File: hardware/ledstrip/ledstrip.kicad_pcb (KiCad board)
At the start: 4 copper layers, 118 parts, among them J1 Conn_ARM_JTAG_SWD_10, J2 USB_C_Receptacle_USB2.0_16P, J4 BMS connectors, J5 Ledstrip connector, J6 Header for STUSB4500 I2C, Q1 Q_NMOS, Q10 Q_PMOS, Q11 Q_NMOS, Q2 Q_NMOS, Q3 Q_NMOS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

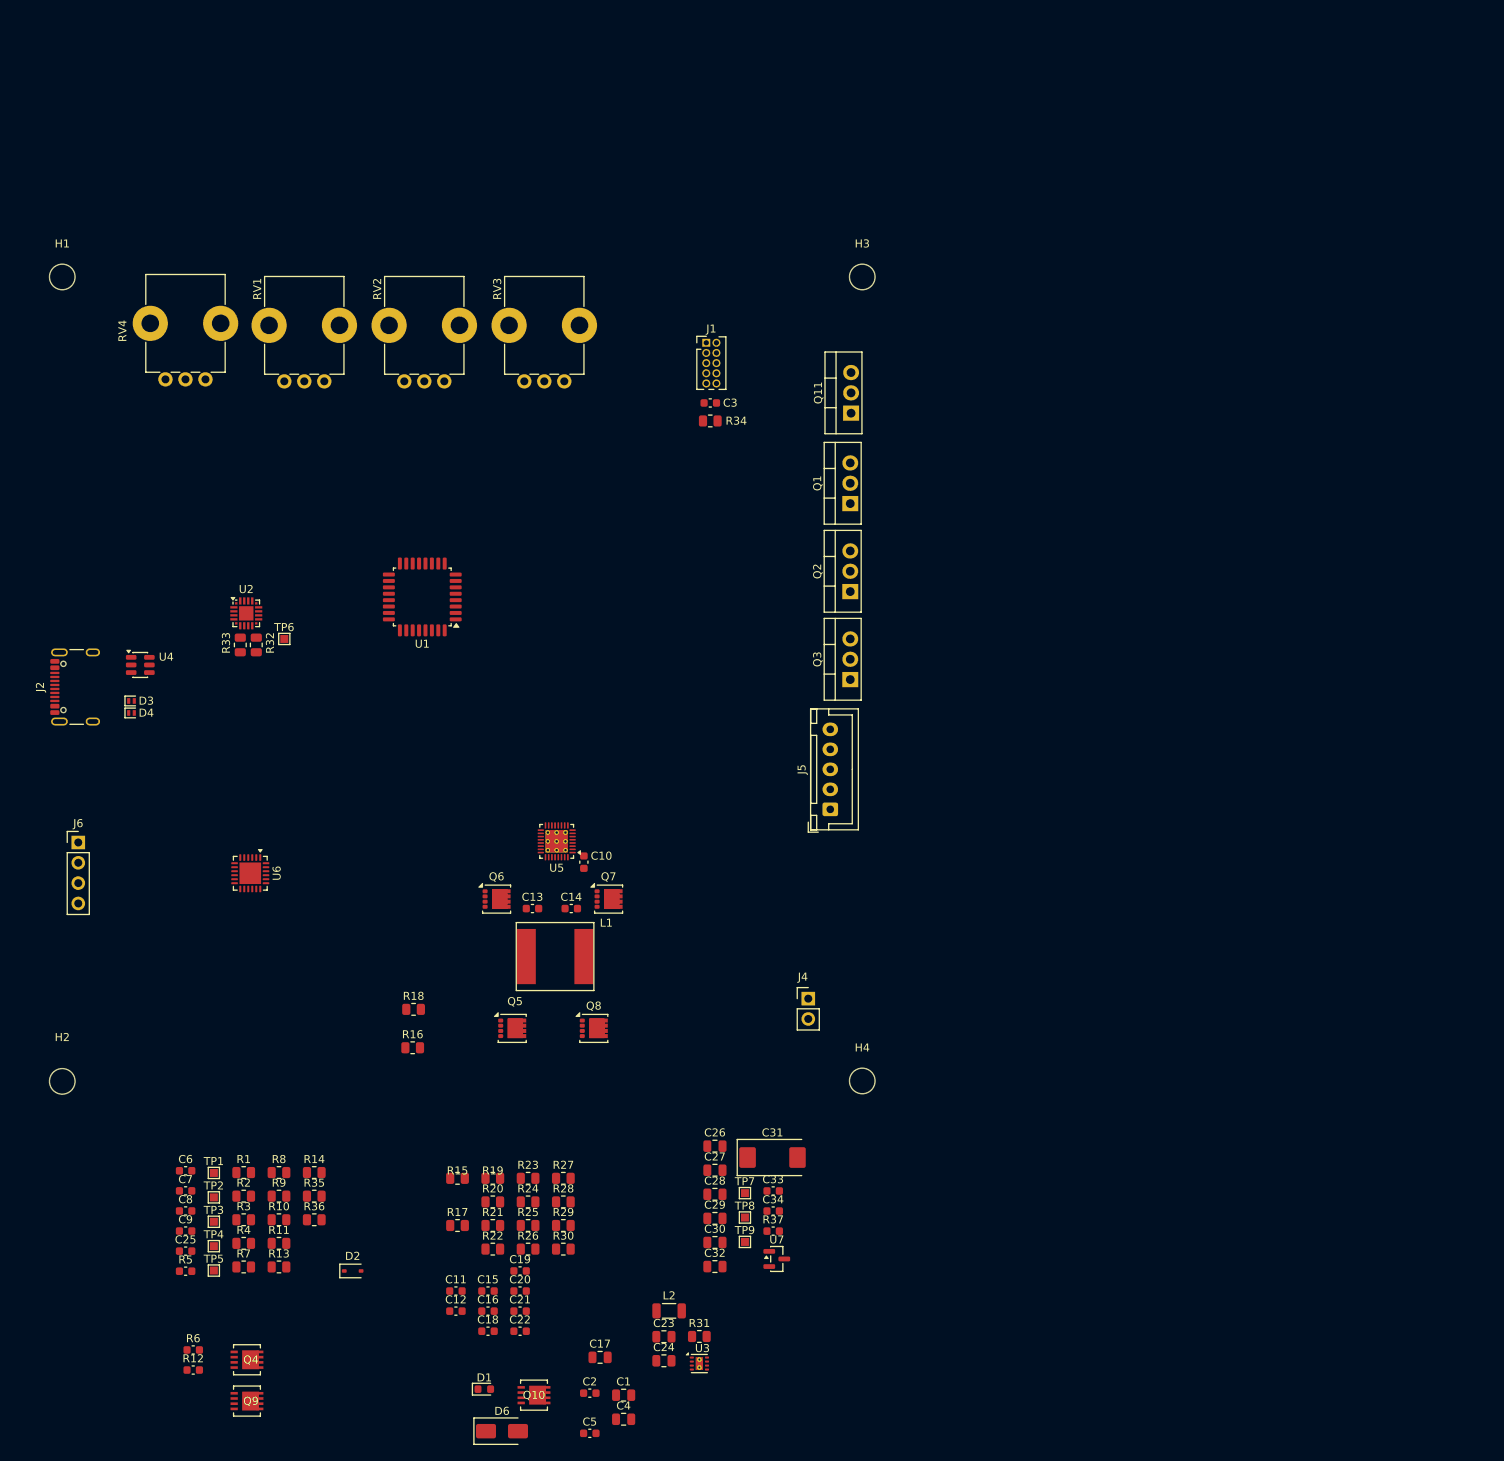
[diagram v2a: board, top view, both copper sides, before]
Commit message: Improve footprint placements.
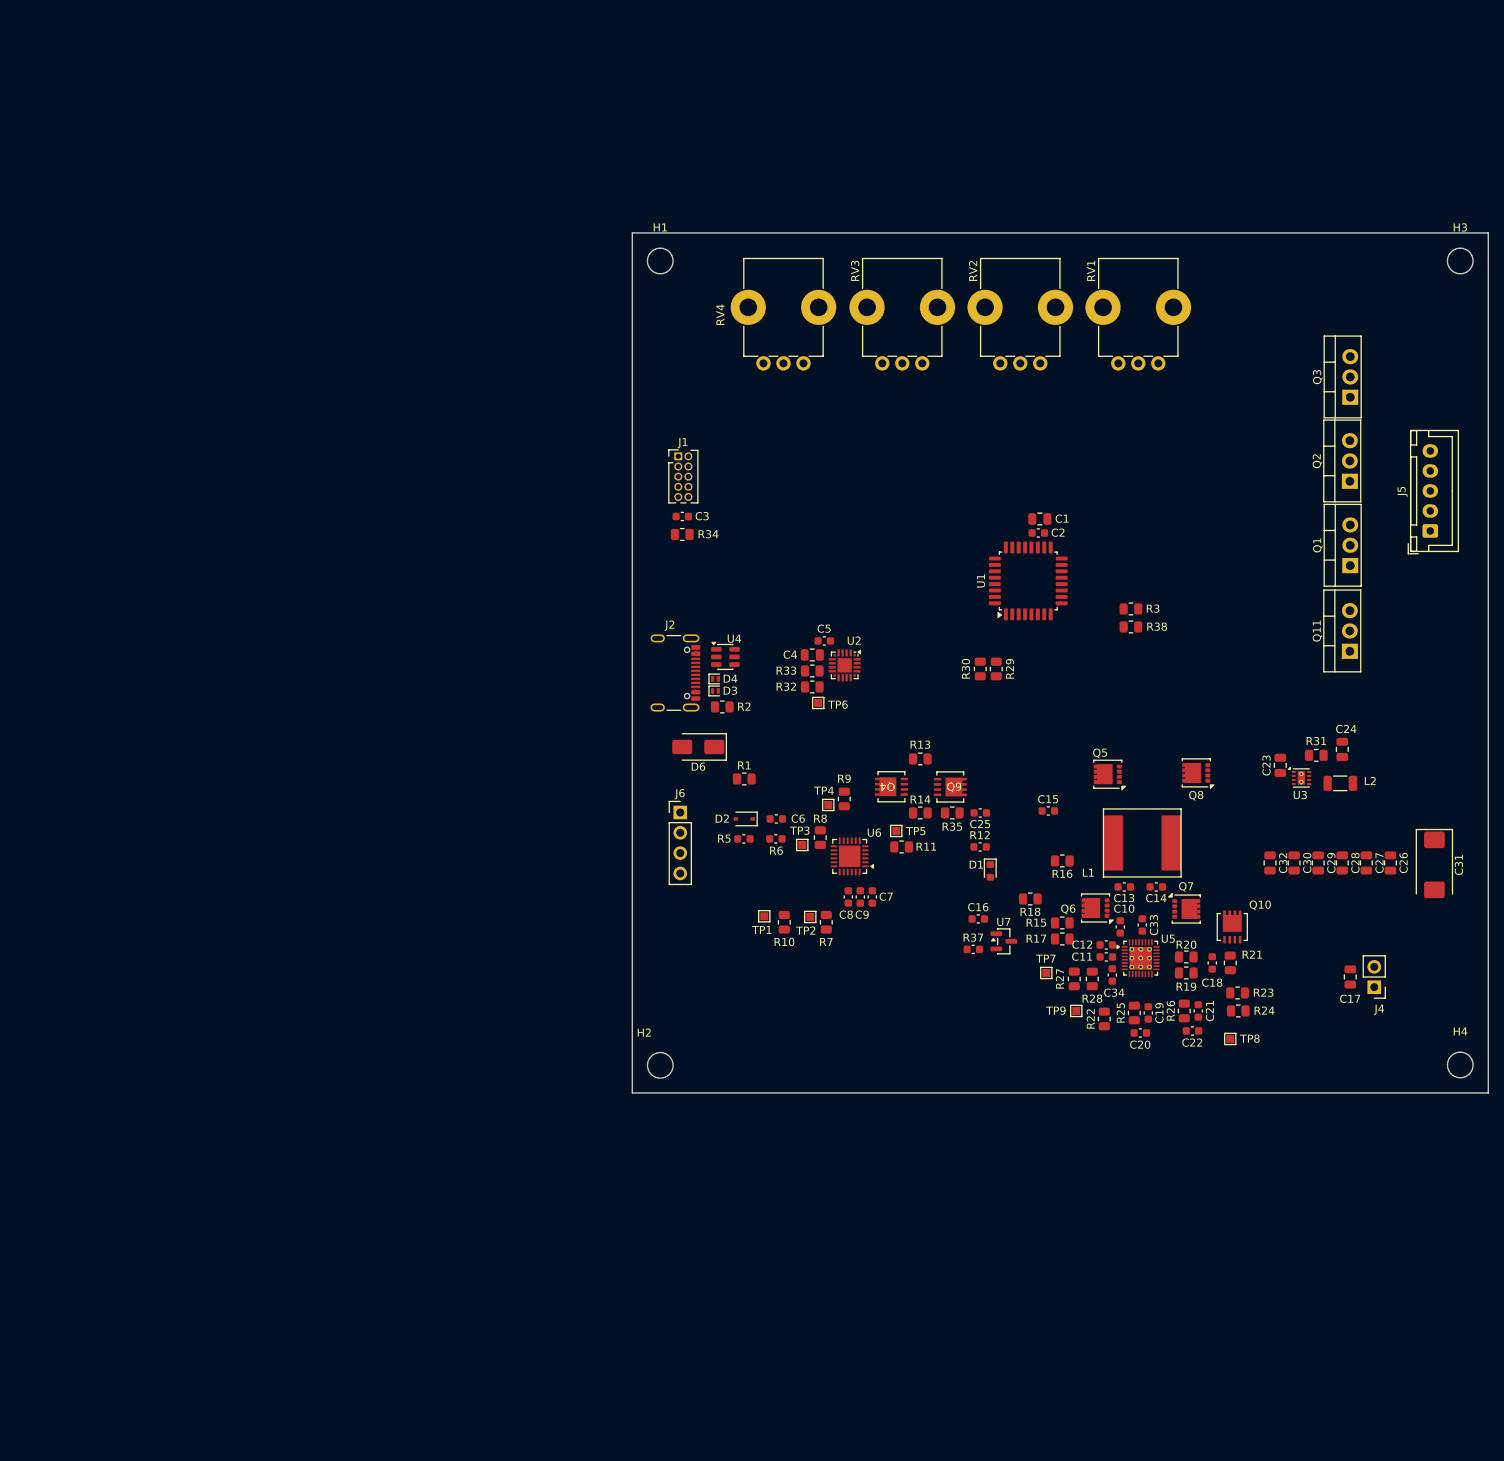
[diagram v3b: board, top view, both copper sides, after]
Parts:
- removed R36: 100K, Resistor_SMD:R_0805_2012Metric
- removed R4: 4,7K, Resistor_SMD:R_0805_2012Metric
- added R38: 10k, Resistor_SMD:R_0805_2012Metric, F.Cu at (158.6, 94.0)
- R3: value 4,7K -> 10k
- moved R3 134.6 mm to (158.6, 91.8)
- moved C2 121.3 mm to (147.0, 82.2)
- moved C1 121.3 mm to (147.2, 80.5)
- moved R12 118.1 mm to (139.7, 121.5)
- moved Q9 116.7 mm to (136.0, 114.0)
- moved C24 114.2 mm to (185.0, 109.3), turned to 90 degrees
- moved C25 113.4 mm to (139.8, 117.2), turned to 180 degrees
- moved Q4 107.8 mm to (128.6, 114.0), turned to 180 degrees
- moved L2 106.7 mm to (184.8, 113.5)
- moved R31 105.9 mm to (181.8, 110.0), turned to 180 degrees
- moved C17 105.1 mm to (186.0, 137.8), turned to -90 degrees
- moved Q10 105.1 mm to (171.2, 131.5), turned to 90 degrees
- moved C23 105.1 mm to (177.2, 111.3), turned to 90 degrees
- moved U3 105.0 mm to (179.9, 112.9)
- moved RV1 104.3 mm to (162.0, 61.0)
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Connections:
- J6 pad 2: /USB PD/STUSB4500_I2C_HEADER_SCL -> /Battery Charger/BQ25703A_SCL
- J6 pad 3: /USB PD/STUSB4500_I2C_HEADER_SDA -> /Battery Charger/BQ25703A_SDA
- R1 pad 2: /USB PD/STUSB4500_VSYS -> +3.3V
- R3 pad 1: /USB PD/STUSB4500_VSYS -> /Battery Charger/BQ25703A_SDA
- R3 pad 2: /USB PD/STUSB4500_I2C_HEADER_SDA -> +3.3V
- U6 pad 24: /USB PD/STUSB4500_VSYS -> +3.3V
- U6 pad 7: /USB PD/STUSB4500_I2C_HEADER_SCL -> /Battery Charger/BQ25703A_SCL
- U6 pad 8: /USB PD/STUSB4500_I2C_HEADER_SDA -> /Battery Charger/BQ25703A_SDA
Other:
- board outline added: 107 x 107.5 mm

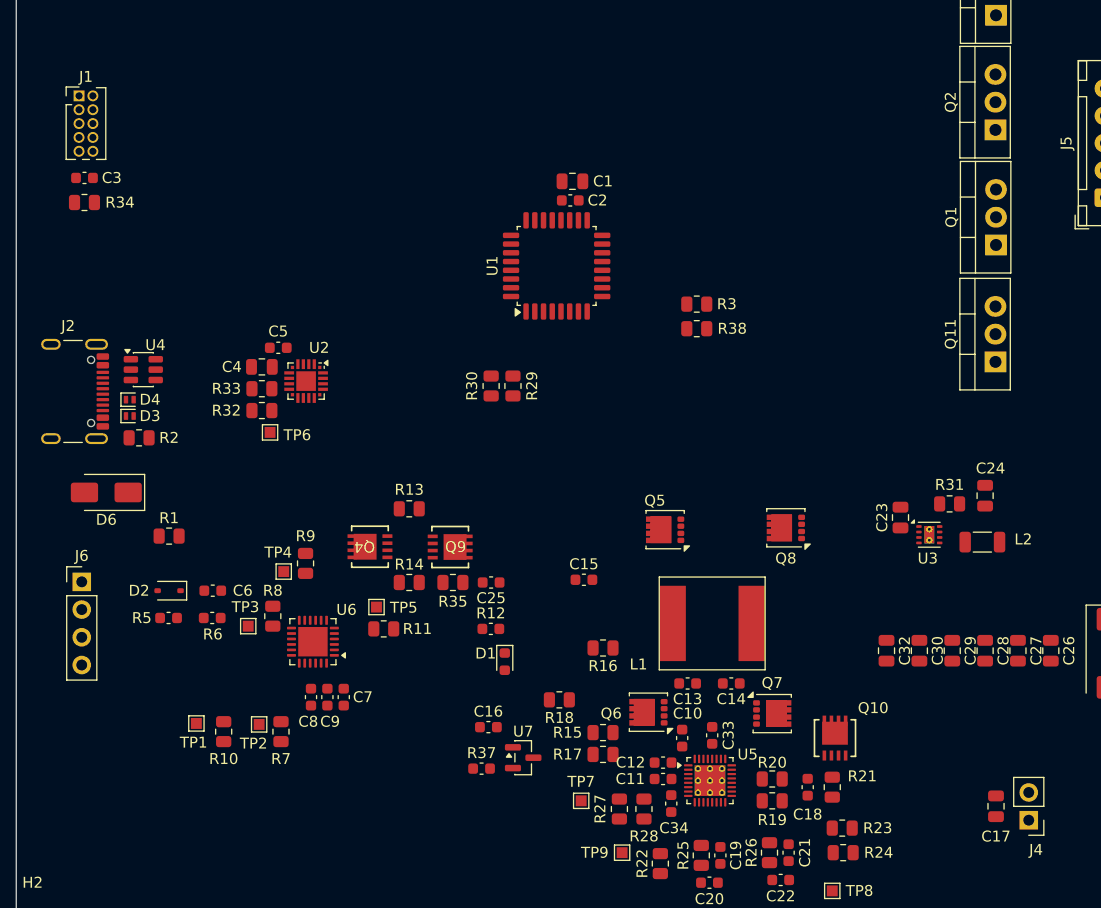
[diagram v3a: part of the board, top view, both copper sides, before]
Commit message: Improve slightly placements.
Add next step in README.md.
Add description of layers usages.
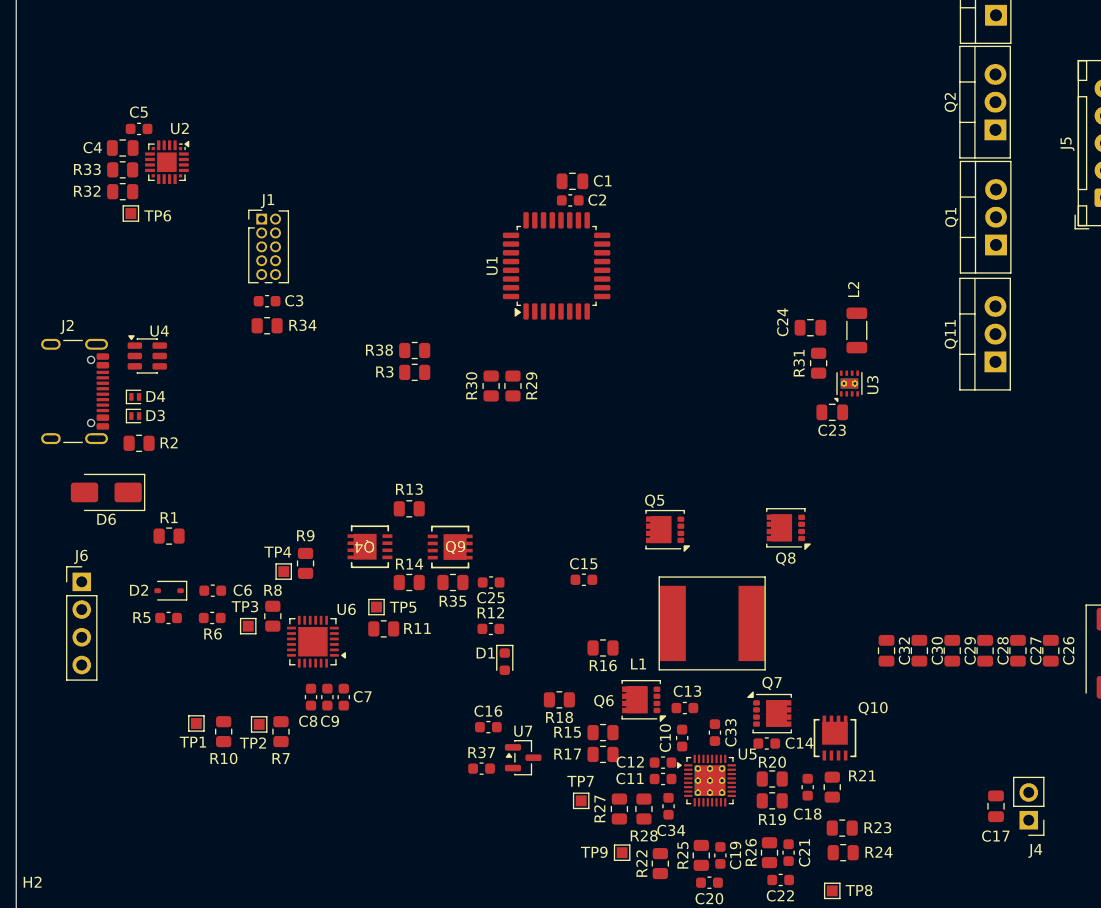
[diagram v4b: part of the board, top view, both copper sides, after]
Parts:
- moved R3 26.6 mm to (132.8, 98.0), turned to 180 degrees
- moved R38 25.9 mm to (132.8, 96.0), turned to 180 degrees
- moved C4 23.8 mm to (106.0, 77.5)
- moved C5 23.8 mm to (107.5, 75.7)
- moved R32 23.8 mm to (106.0, 81.5)
- moved R33 23.8 mm to (106.0, 79.5)
- moved TP6 23.8 mm to (106.8, 83.5)
- moved U2 23.8 mm to (110.0, 78.8)
- moved L2 22.5 mm to (173.2, 94.2), turned to 90 degrees
- moved C24 22.2 mm to (169.0, 93.9), turned to 180 degrees
- moved C3 20.2 mm to (119.2, 91.5)
- moved R34 20.2 mm to (119.2, 93.7)
- moved J1 20.2 mm to (118.7, 84.0)
- moved R31 17.6 mm to (169.8, 97.2), turned to -90 degrees
- moved U3 15.7 mm to (172.6, 99.0), turned to 90 degrees
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
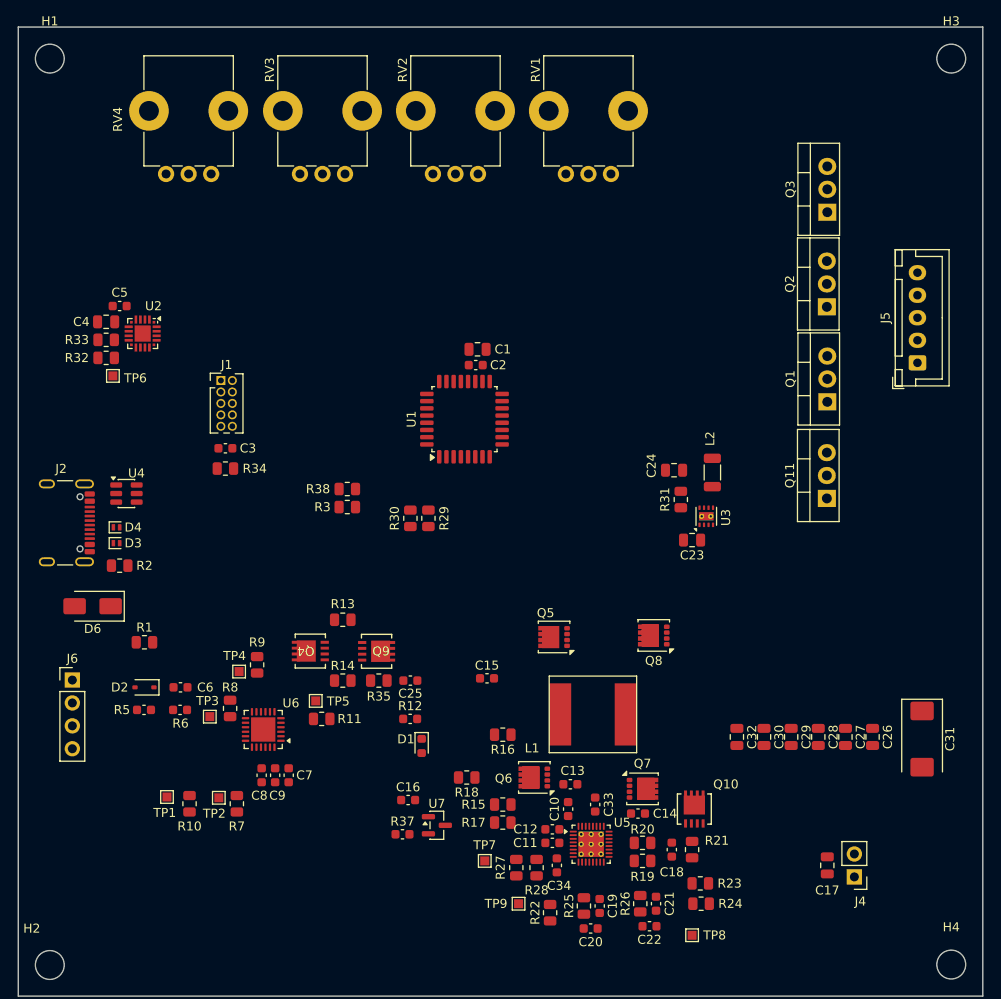
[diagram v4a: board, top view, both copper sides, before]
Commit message: Added GND zone in L2 layer + vias for ground.
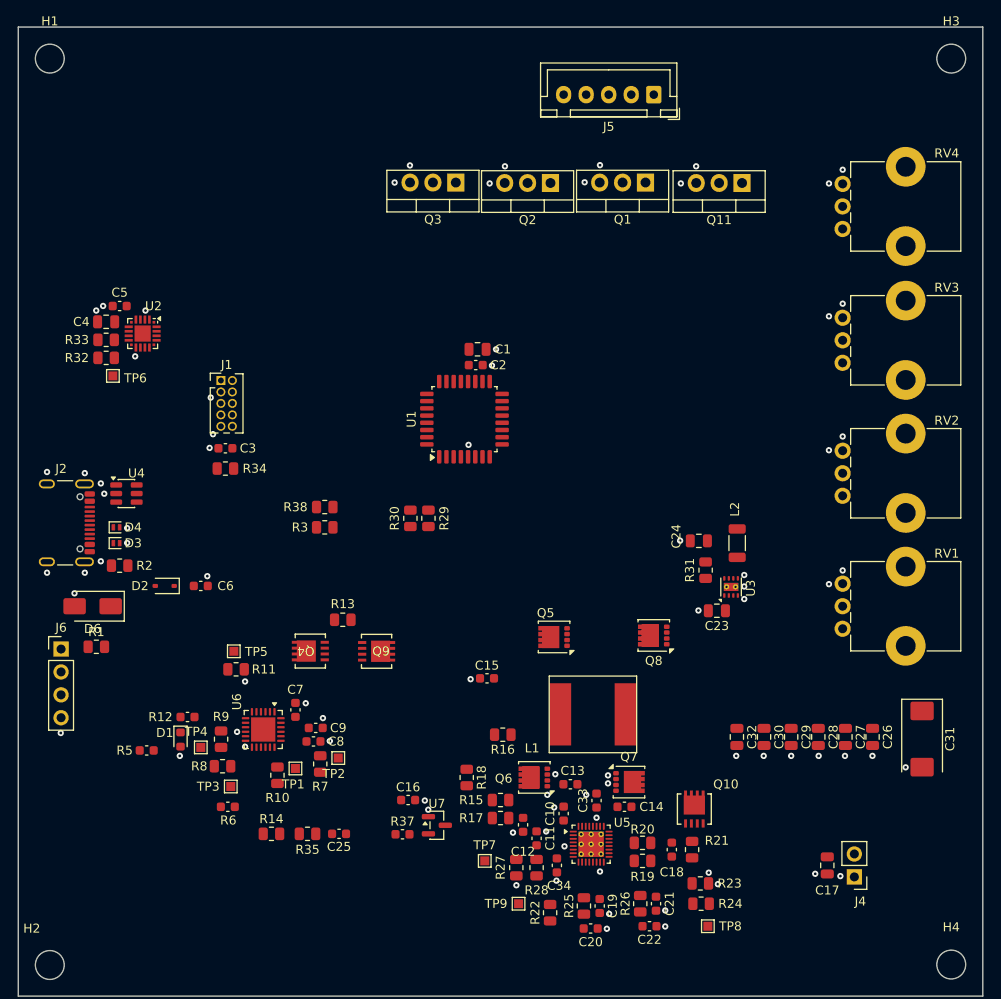
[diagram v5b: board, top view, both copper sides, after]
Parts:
- moved RV4 70.3 mm to (187.7, 67.2), turned to 0 degrees
- moved RV3 59.0 mm to (187.7, 82.0), turned to 0 degrees
- moved RV1 56.6 mm to (187.7, 111.5), turned to 0 degrees
- moved RV2 54.0 mm to (187.7, 96.8), turned to 0 degrees
- moved J5 41.7 mm to (166.8, 52.2), turned to 180 degrees
- moved Q3 41.3 mm to (144.8, 62.0), turned to 180 degrees
- moved Q11 36.2 mm to (176.5, 62.0), turned to 180 degrees
- moved Q2 33.6 mm to (155.3, 62.0), turned to 180 degrees
- moved Q1 31.6 mm to (165.8, 62.0), turned to 180 degrees
- moved D1 26.8 mm to (114.2, 123.8)
- moved R12 24.7 mm to (115.0, 121.3)
- moved C25 18.8 mm to (131.8, 134.2)
- moved R14 18.8 mm to (124.3, 134.2)
- moved R35 18.8 mm to (128.3, 134.2)
- moved TP1 14.6 mm to (127.0, 127.0)
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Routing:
- net GND: vias 0 -> 81
- added copper zone on In1.Cu, net GND
